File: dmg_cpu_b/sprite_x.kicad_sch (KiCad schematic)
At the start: 88 parts

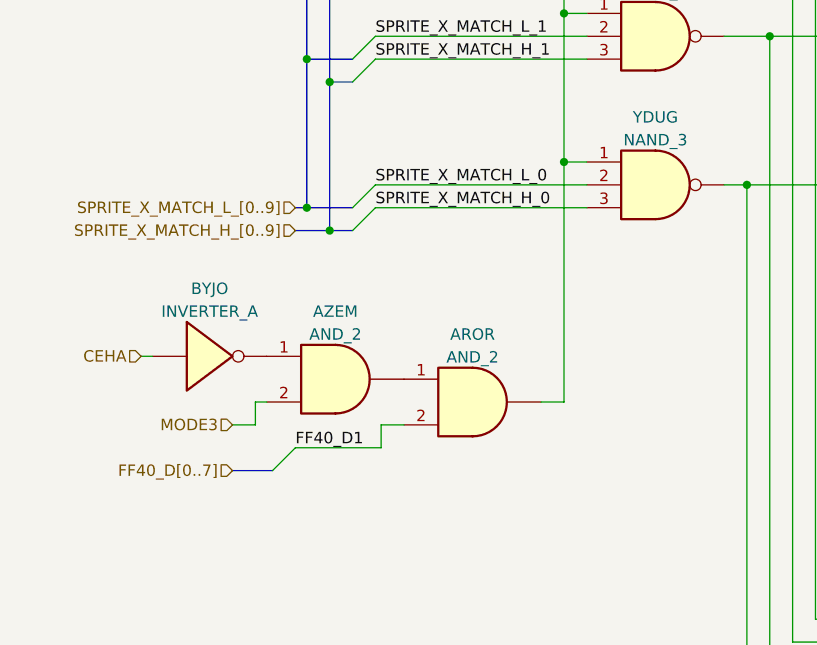
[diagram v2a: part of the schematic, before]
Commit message: More OAM sheets added.
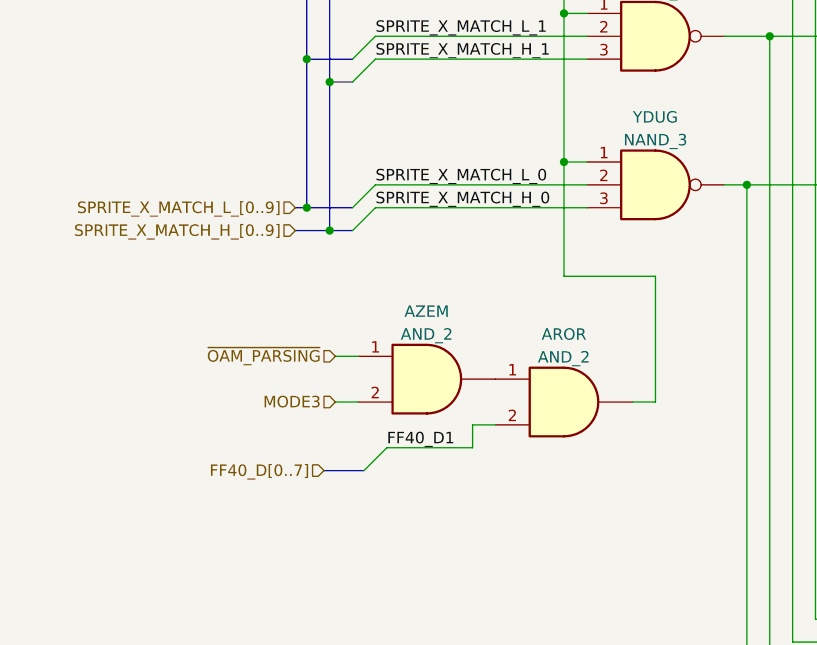
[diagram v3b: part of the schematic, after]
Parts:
- removed BYJO: INVERTER_A, symbol DMG_CPU_Cells:INVERTER_A
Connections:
- net ~{OAM_PARSING}: now reaches AZEM.1
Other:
- moved on the sheet: AROR, AZEM
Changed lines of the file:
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@@
   (junction (at 275.59 61.595) (diameter 0) (color 0 0 0 0)
   )
+  (junction (at 69.215 191.135) (diameter 0) (color 0 0 0 0)
+  )
   (junction (at 40.64 113.665) (diameter 0) (color 0 0 0 0)
   )
@@
   )
   (junction (at 115.57 193.675) (diameter 0) (color 0 0 0 0)
-  )
-  (junction (at 69.215 191.135) (diameter 0) (color 0 0 0 0)
   )
   (junction (at 69.215 92.075) (diameter 0) (color 0 0 0 0)
@@
     (stroke (width 0) (type default) (color 0 0 0 0))
   )
-  (bus_entry (at 39.37 222.885) (size -2.54 2.54)
+  (bus_entry (at 49.53 222.885) (size -2.54 2.54)
     (stroke (width 0) (type default) (color 0 0 0 0))
   )
@@
     (stroke (width 0) (type default) (color 0 0 0 0))
   )
-  (wire (pts (xy 66.675 217.805) (xy 69.215 217.805))
-    (stroke (width 0) (type default) (color 0 0 0 0))
-  )
   (wire (pts (xy 381.635 202.565) (xy 368.3 202.565))
     (stroke (width 0) (type default) (color 0 0 0 0))
@@
     (stroke (width 0) (type default) (color 0 0 0 0))
   )
-  (wire (pts (xy 32.385 220.345) (xy 34.925 220.345))
-    (stroke (width 0) (type default) (color 0 0 0 0))
-  )
   (wire (pts (xy 275.59 73.025) (xy 278.13 73.025))
     (stroke (width 0) (type default) (color 0 0 0 0))
@@
     (stroke (width 0) (type default) (color 0 0 0 0))
   )
+  (wire (pts (xy 79.375 203.835) (xy 79.375 217.805))
+    (stroke (width 0) (type default) (color 0 0 0 0))
+  )
   (wire (pts (xy 312.42 108.585) (xy 312.42 92.075))
     (stroke (width 0) (type default) (color 0 0 0 0))
@@
     (stroke (width 0) (type default) (color 0 0 0 0))
   )
+  (wire (pts (xy 79.375 217.805) (xy 76.835 217.805))
+    (stroke (width 0) (type default) (color 0 0 0 0))
+  )
   (wire (pts (xy 69.215 141.605) (xy 69.215 125.095))
     (stroke (width 0) (type default) (color 0 0 0 0))
@@
     (stroke (width 0) (type default) (color 0 0 0 0))
   )
-  (wire (pts (xy 34.925 220.345) (xy 34.925 217.805))
+  (wire (pts (xy 43.815 217.805) (xy 46.355 217.805))
     (stroke (width 0) (type default) (color 0 0 0 0))
   )
@@
     (stroke (width 0) (type default) (color 0 0 0 0))
   )
-  (wire (pts (xy 22.225 212.725) (xy 23.495 212.725))
+  (wire (pts (xy 43.815 212.725) (xy 46.355 212.725))
     (stroke (width 0) (type default) (color 0 0 0 0))
   )
@@
     (stroke (width 0) (type default) (color 0 0 0 0))
   )
+  (wire (pts (xy 69.215 203.835) (xy 79.375 203.835))
+    (stroke (width 0) (type default) (color 0 0 0 0))
+  )
   (wire (pts (xy 335.28 155.575) (xy 340.36 155.575))
     (stroke (width 0) (type default) (color 0 0 0 0))
@@
     (stroke (width 0) (type default) (color 0 0 0 0))
   )
-  (wire (pts (xy 34.925 217.805) (xy 36.195 217.805))
-    (stroke (width 0) (type default) (color 0 0 0 0))
-  )
   (wire (pts (xy 48.26 160.655) (xy 71.755 160.655))
     (stroke (width 0) (type default) (color 0 0 0 0))
@@
     (stroke (width 0) (type default) (color 0 0 0 0))
   )
-  (bus (pts (xy 32.385 225.425) (xy 36.83 225.425))
+  (bus (pts (xy 42.545 225.425) (xy 46.99 225.425))
     (stroke (width 0) (type default) (color 0 0 0 0))
   )
@@
     (stroke (width 0) (type default) (color 0 0 0 0))
   )
-  (wire (pts (xy 39.37 222.885) (xy 48.895 222.885))
+  (wire (pts (xy 49.53 222.885) (xy 59.055 222.885))
     (stroke (width 0) (type default) (color 0 0 0 0))
   )
@@
     (stroke (width 0) (type default) (color 0 0 0 0))
   )
-  (wire (pts (xy 51.435 220.345) (xy 48.895 220.345))
+  (wire (pts (xy 61.595 220.345) (xy 59.055 220.345))
     (stroke (width 0) (type default) (color 0 0 0 0))
   )
@@
     (stroke (width 0) (type default) (color 0 0 0 0))
   )
-  (wire (pts (xy 69.215 217.805) (xy 69.215 191.135))
-    (stroke (width 0) (type default) (color 0 0 0 0))
-  )
   (wire (pts (xy 71.755 75.565) (xy 69.215 75.565))
     (stroke (width 0) (type default) (color 0 0 0 0))
@@
     (stroke (width 0) (type default) (color 0 0 0 0))
   )
+  (wire (pts (xy 69.215 191.135) (xy 69.215 203.835))
+    (stroke (width 0) (type default) (color 0 0 0 0))
+  )
   (wire (pts (xy 151.13 186.055) (xy 129.54 186.055))
     (stroke (width 0) (type default) (color 0 0 0 0))
@@
     (stroke (width 0) (type default) (color 0 0 0 0))
   )
-  (wire (pts (xy 48.895 220.345) (xy 48.895 222.885))
+  (wire (pts (xy 59.055 220.345) (xy 59.055 222.885))
     (stroke (width 0) (type default) (color 0 0 0 0))
   )
@@
     (stroke (width 0) (type default) (color 0 0 0 0))
   )
-  (label "FF40_D1" (at 39.37 222.885 0)
+  (label "FF40_D1" (at 49.53 222.885 0)
     (effects (font (size 1.27 1.27)) (justify left bottom))
   )
@@
     (effects (font (size 1.27 1.27)) (justify left))
   )
-  (hierarchical_label "CEHA" (shape input) (at 22.225 212.725 180)
+  (hierarchical_label "~{OAM_PARSING}" (shape input) (at 43.815 212.725 180)
     (effects (font (size 1.27 1.27)) (justify right))
   )
@@
     (effects (font (size 1.27 1.27)) (justify left))
   )
-  (hierarchical_label "FF40_D[0..7]" (shape input) (at 32.385 225.425 180)
+  (hierarchical_label "FF40_D[0..7]" (shape input) (at 42.545 225.425 180)
     (effects (font (size 1.27 1.27)) (justify right))
   )
-  (hierarchical_label "MODE3" (shape input) (at 32.385 220.345 180)
+  (hierarchical_label "MODE3" (shape input) (at 43.815 217.805 180)
     (effects (font (size 1.27 1.27)) (justify right))
   )
@@
     (pin "6")
   )
-  (symbol (lib_id "DMG_CPU_Cells:INVERTER_A") (at 29.845 212.725 0) (unit 1)
-    (in_bom yes) (on_board yes) (fields_autoplaced)
-    (property "Reference" "BYJO" (id 0) (at 29.845 205.2152 0))
-    (property "Value" "INVERTER_A" (id 1) (at 29.845 207.7521 0))
-    (property "Footprint" "" (id 2) (at 27.305 212.725 0)
-      (effects (font (size 1.27 1.27)) hide)
-    )
-    (property "Datasheet" "http://iceboy.a-singer.de/doc/dmg_cells.html#inv_a" (id 3) (at 31.115 220.345 0)
-      (effects (font (size 1.27 1.27)) hide)
-    )
-    (pin "1")
-    (pin "2")
-  )
   (symbol (lib_id "DMG_CPU_Cells:NAND_3") (at 79.375 144.145 0) (unit 1)
     (in_bom yes) (on_board yes) (fields_autoplaced)
@@
     (pin "4")
   )
-  (symbol (lib_id "DMG_CPU_Cells:AND_2") (at 59.055 217.805 0) (unit 1)
-    (in_bom yes) (on_board yes) (fields_autoplaced)
-    (property "Reference" "AROR" (id 0) (at 59.055 210.2952 0))
-    (property "Value" "AND_2" (id 1) (at 59.055 212.8321 0))
-    (property "Footprint" "" (id 2) (at 59.055 217.805 0)
-      (effects (font (size 1.27 1.27)) hide)
-    )
-    (property "Datasheet" "http://iceboy.a-singer.de/doc/dmg_cells.html#and2" (id 3) (at 59.055 225.425 0)
+  (symbol (lib_id "DMG_CPU_Cells:AND_2") (at 69.215 217.805 0) (unit 1)
+    (in_bom yes) (on_board yes) (fields_autoplaced)
+    (property "Reference" "AROR" (id 0) (at 69.215 210.2952 0))
+    (property "Value" "AND_2" (id 1) (at 69.215 212.8321 0))
+    (property "Footprint" "" (id 2) (at 69.215 217.805 0)
+      (effects (font (size 1.27 1.27)) hide)
+    )
+    (property "Datasheet" "http://iceboy.a-singer.de/doc/dmg_cells.html#and2" (id 3) (at 69.215 225.425 0)
       (effects (font (size 1.27 1.27)) hide)
     )
@@
     (pin "2")
   )
-  (symbol (lib_id "DMG_CPU_Cells:AND_2") (at 43.815 215.265 0) (unit 1)
-    (in_bom yes) (on_board yes) (fields_autoplaced)
-    (property "Reference" "AZEM" (id 0) (at 43.815 207.7552 0))
-    (property "Value" "AND_2" (id 1) (at 43.815 210.2921 0))
-    (property "Footprint" "" (id 2) (at 43.815 215.265 0)
-      (effects (font (size 1.27 1.27)) hide)
-    )
-    (property "Datasheet" "http://iceboy.a-singer.de/doc/dmg_cells.html#and2" (id 3) (at 43.815 222.885 0)
-      (effects (font (size 1.27 1.27)) hide)
-    )
+  (symbol (lib_id "DMG_CPU_Cells:AND_2") (at 53.975 215.265 0) (unit 1)
+    (in_bom yes) (on_board yes) (fields_autoplaced)
+    (property "Reference" "AZEM" (id 0) (at 53.975 207.7552 0))
+    (property "Value" "AND_2" (id 1) (at 53.975 210.2921 0))
+    (property "Footprint" "" (id 2) (at 53.975 215.265 0)
+      (effects (font (size 1.27 1.27)) hide)
+    )
+    (property "Datasheet" "http://iceboy.a-singer.de/doc/dmg_cells.html#and2" (id 3) (at 53.975 222.885 0)
+      (effects (font (size 1.27 1.27)) hide)
+    )

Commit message: All sheets captured. Serious tidying is required in PPU section.
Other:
- company: (none) -> CC-BY-SA-4.0 Régis Galland & Michael Singer -- Derived work from Furrtek
- title: (none) -> DMG CPU B
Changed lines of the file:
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@@
 (kicad_sch (version 20211123) (generator eeschema)
   (paper "A3")
+  (title_block
+    (title "DMG CPU B")
+    (date "2022-05-19")
+    (rev "0")
+    (company "CC-BY-SA-4.0 Régis Galland & Michael Singer -- Derived work from Furrtek")
+    (comment 1 "https://github.com/msinger/dmg-schematics")
+  )
   (junction (at 337.82 100.965) (diameter 0) (color 0 0 0 0)
   )

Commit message: Changes made on review.
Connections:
- net ~{RESET_VIDEO} renamed ~{PPU_RESET}
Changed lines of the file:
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@@
     (effects (font (size 1.27 1.27)) (justify right))
   )
-  (hierarchical_label "~{RESET_VIDEO}" (shape input) (at 256.54 34.29 180)
+  (hierarchical_label "~{PPU_RESET}" (shape input) (at 256.54 34.29 180)
     (effects (font (size 1.27 1.27)) (justify right))
   )

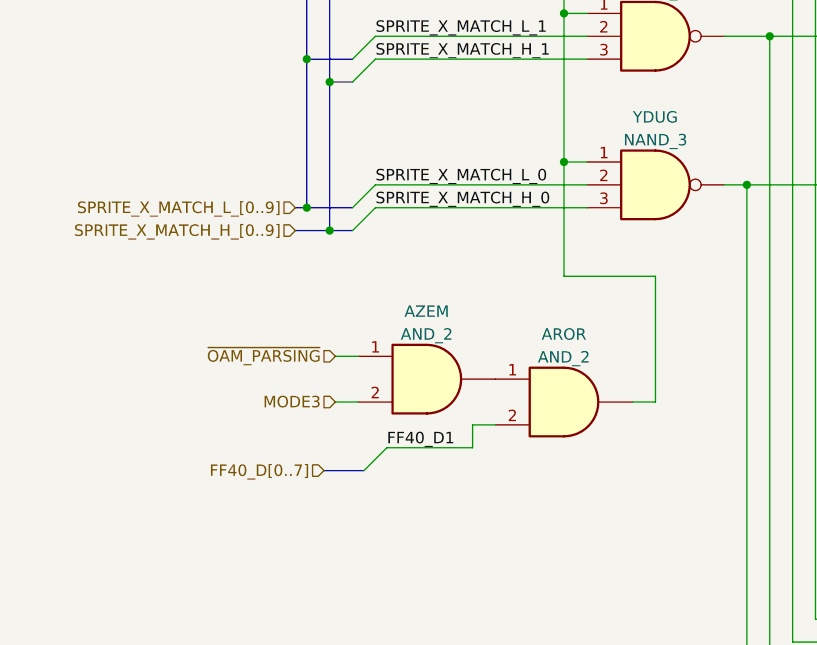
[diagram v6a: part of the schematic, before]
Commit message: Elements from sptite control sheet moved to lcd sheet.
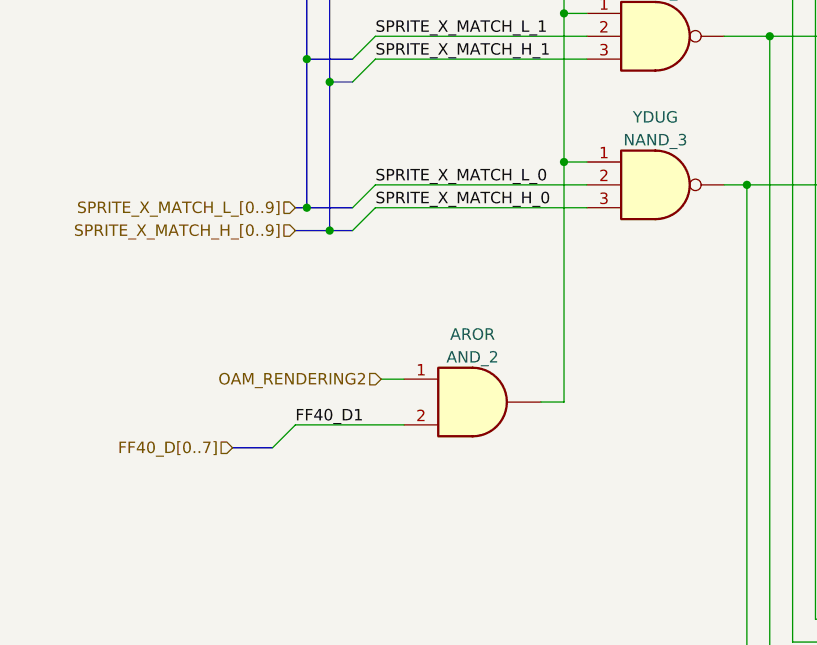
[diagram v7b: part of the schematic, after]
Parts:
- removed AZEM: AND_2, symbol DMG_CPU_Cells:AND_2
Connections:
- net OAM_RENDERING2: now reaches AROR.1
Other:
- moved on the sheet: AROR
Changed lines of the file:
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@@
     (stroke (width 0) (type default) (color 0 0 0 0))
   )
-  (bus_entry (at 49.53 222.885) (size -2.54 2.54)
+  (bus_entry (at 39.37 220.345) (size -2.54 2.54)
     (stroke (width 0) (type default) (color 0 0 0 0))
   )
@@
     (stroke (width 0) (type default) (color 0 0 0 0))
   )
-  (wire (pts (xy 79.375 203.835) (xy 79.375 217.805))
-    (stroke (width 0) (type default) (color 0 0 0 0))
-  )
   (wire (pts (xy 312.42 108.585) (xy 312.42 92.075))
     (stroke (width 0) (type default) (color 0 0 0 0))
@@
     (stroke (width 0) (type default) (color 0 0 0 0))
   )
-  (wire (pts (xy 79.375 217.805) (xy 76.835 217.805))
+  (wire (pts (xy 69.215 217.805) (xy 66.675 217.805))
     (stroke (width 0) (type default) (color 0 0 0 0))
   )
@@
     (stroke (width 0) (type default) (color 0 0 0 0))
   )
-  (wire (pts (xy 43.815 217.805) (xy 46.355 217.805))
-    (stroke (width 0) (type default) (color 0 0 0 0))
-  )
   (wire (pts (xy 220.98 103.505) (xy 220.98 108.585))
     (stroke (width 0) (type default) (color 0 0 0 0))
@@
     (stroke (width 0) (type default) (color 0 0 0 0))
   )
-  (wire (pts (xy 43.815 212.725) (xy 46.355 212.725))
+  (wire (pts (xy 48.895 215.265) (xy 51.435 215.265))
     (stroke (width 0) (type default) (color 0 0 0 0))
   )
@@
     (stroke (width 0) (type default) (color 0 0 0 0))
   )
-  (wire (pts (xy 69.215 203.835) (xy 79.375 203.835))
-    (stroke (width 0) (type default) (color 0 0 0 0))
-  )
   (wire (pts (xy 335.28 155.575) (xy 340.36 155.575))
     (stroke (width 0) (type default) (color 0 0 0 0))
@@
     (stroke (width 0) (type default) (color 0 0 0 0))
   )
-  (bus (pts (xy 42.545 225.425) (xy 46.99 225.425))
+  (bus (pts (xy 32.385 222.885) (xy 36.83 222.885))
     (stroke (width 0) (type default) (color 0 0 0 0))
   )
@@
     (stroke (width 0) (type default) (color 0 0 0 0))
   )
-  (wire (pts (xy 49.53 222.885) (xy 59.055 222.885))
-    (stroke (width 0) (type default) (color 0 0 0 0))
-  )
   (wire (pts (xy 275.59 127.635) (xy 275.59 122.555))
     (stroke (width 0) (type default) (color 0 0 0 0))
@@
     (stroke (width 0) (type default) (color 0 0 0 0))
   )
-  (wire (pts (xy 61.595 220.345) (xy 59.055 220.345))
+  (wire (pts (xy 39.37 220.345) (xy 51.435 220.345))
     (stroke (width 0) (type default) (color 0 0 0 0))
   )
@@
     (stroke (width 0) (type default) (color 0 0 0 0))
   )
-  (wire (pts (xy 69.215 191.135) (xy 69.215 203.835))
+  (wire (pts (xy 69.215 191.135) (xy 69.215 217.805))
     (stroke (width 0) (type default) (color 0 0 0 0))
   )
@@
     (stroke (width 0) (type default) (color 0 0 0 0))
   )
-  (wire (pts (xy 59.055 220.345) (xy 59.055 222.885))
-    (stroke (width 0) (type default) (color 0 0 0 0))
-  )
   (wire (pts (xy 275.59 94.615) (xy 275.59 89.535))
     (stroke (width 0) (type default) (color 0 0 0 0))
@@
     (stroke (width 0) (type default) (color 0 0 0 0))
   )
-  (label "FF40_D1" (at 49.53 222.885 0)
+  (label "FF40_D1" (at 39.37 220.345 0)
     (effects (font (size 1.27 1.27)) (justify left bottom))
   )
@@
     (effects (font (size 1.27 1.27)) (justify left))
   )
-  (hierarchical_label "~{OAM_PARSING}" (shape input) (at 43.815 212.725 180)
+  (hierarchical_label "OAM_RENDERING2" (shape input) (at 48.895 215.265 180)
     (effects (font (size 1.27 1.27)) (justify right))
   )
@@
     (effects (font (size 1.27 1.27)) (justify left))
   )
-  (hierarchical_label "FF40_D[0..7]" (shape input) (at 42.545 225.425 180)
-    (effects (font (size 1.27 1.27)) (justify right))
-  )
-  (hierarchical_label "MODE3" (shape input) (at 43.815 217.805 180)
+  (hierarchical_label "FF40_D[0..7]" (shape input) (at 32.385 222.885 180)
     (effects (font (size 1.27 1.27)) (justify right))
   )
@@
     (pin "4")
   )
-  (symbol (lib_id "DMG_CPU_Cells:AND_2") (at 69.215 217.805 0) (unit 1)
-    (in_bom yes) (on_board yes) (fields_autoplaced)
-    (property "Reference" "AROR" (id 0) (at 69.215 210.2952 0))
-    (property "Value" "AND_2" (id 1) (at 69.215 212.8321 0))
-    (property "Footprint" "" (id 2) (at 69.215 217.805 0)
-      (effects (font (size 1.27 1.27)) hide)
-    )
-    (property "Datasheet" "http://iceboy.a-singer.de/doc/dmg_cells.html#and2" (id 3) (at 69.215 225.425 0)
+  (symbol (lib_id "DMG_CPU_Cells:AND_2") (at 59.055 217.805 0) (unit 1)
+    (in_bom yes) (on_board yes) (fields_autoplaced)
+    (property "Reference" "AROR" (id 0) (at 59.055 210.2952 0))
+    (property "Value" "AND_2" (id 1) (at 59.055 212.8321 0))
+    (property "Footprint" "" (id 2) (at 59.055 217.805 0)
+      (effects (font (size 1.27 1.27)) hide)
+    )
+    (property "Datasheet" "http://iceboy.a-singer.de/doc/dmg_cells.html#and2" (id 3) (at 59.055 225.425 0)
       (effects (font (size 1.27 1.27)) hide)
     )
@@
     (pin "2")
   )
-  (symbol (lib_id "DMG_CPU_Cells:AND_2") (at 53.975 215.265 0) (unit 1)
-    (in_bom yes) (on_board yes) (fields_autoplaced)
-    (property "Reference" "AZEM" (id 0) (at 53.975 207.7552 0))
-    (property "Value" "AND_2" (id 1) (at 53.975 210.2921 0))
-    (property "Footprint" "" (id 2) (at 53.975 215.265 0)
-      (effects (font (size 1.27 1.27)) hide)
-    )
-    (property "Datasheet" "http://iceboy.a-singer.de/doc/dmg_cells.html#and2" (id 3) (at 53.975 222.885 0)
-      (effects (font (size 1.27 1.27)) hide)
-    )
-    (pin "1")
-    (pin "2")
-    (pin "3")
-  )
   (symbol (lib_id "DMG_CPU_Cells:OR_2") (at 236.22 80.645 0) (unit 1)

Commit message: Quite a few fixes from review.
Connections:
- net at FEFY.6: now also FEPO.1; no longer FEPO.2
- net at FOVE.6: now also FEPO.2; no longer FEPO.1
- net SPRITE_RST_0 renamed SPRITE_RST0
- net SPRITE_RST_1 renamed SPRITE_RST1
- net SPRITE_RST_2 renamed SPRITE_RST2
- net SPRITE_RST_3 renamed SPRITE_RST3
- net SPRITE_RST_4 renamed SPRITE_RST4
- net SPRITE_RST_5 renamed SPRITE_RST5
- net SPRITE_RST_6 renamed SPRITE_RST6
- net SPRITE_RST_7 renamed SPRITE_RST7
- net SPRITE_RST_8 renamed SPRITE_RST8
- net SPRITE_RST_9 renamed SPRITE_RST9
- net SPRITE_SEL_0 renamed SPRITE_SEL0
- net SPRITE_SEL_1 renamed SPRITE_SEL1
- net SPRITE_SEL_2 renamed SPRITE_SEL2
- net SPRITE_SEL_3 renamed SPRITE_SEL3
- net SPRITE_SEL_4 renamed SPRITE_SEL4
- net SPRITE_SEL_5 renamed SPRITE_SEL5
- net SPRITE_SEL_6 renamed SPRITE_SEL6
- net SPRITE_SEL_7 renamed SPRITE_SEL7
- net SPRITE_SEL_8 renamed SPRITE_SEL8
- net SPRITE_SEL_9 renamed SPRITE_SEL9
- net SPRITE_X_MATCH_H_0 renamed SPRITE_X_MATCH_H0
- net SPRITE_X_MATCH_H_1 renamed SPRITE_X_MATCH_H1
- net SPRITE_X_MATCH_H_2 renamed SPRITE_X_MATCH_H2
- net SPRITE_X_MATCH_H_3 renamed SPRITE_X_MATCH_H3
- net SPRITE_X_MATCH_H_4 renamed SPRITE_X_MATCH_H4
- net SPRITE_X_MATCH_H_5 renamed SPRITE_X_MATCH_H5
- net SPRITE_X_MATCH_H_6 renamed SPRITE_X_MATCH_H6
- net SPRITE_X_MATCH_H_7 renamed SPRITE_X_MATCH_H7
- net SPRITE_X_MATCH_H_8 renamed SPRITE_X_MATCH_H8
- net SPRITE_X_MATCH_H_9 renamed SPRITE_X_MATCH_H9
- net SPRITE_X_MATCH_L_0 renamed SPRITE_X_MATCH_L0
- net SPRITE_X_MATCH_L_1 renamed SPRITE_X_MATCH_L1
- net SPRITE_X_MATCH_L_2 renamed SPRITE_X_MATCH_L2
- net SPRITE_X_MATCH_L_3 renamed SPRITE_X_MATCH_L3
- net SPRITE_X_MATCH_L_4 renamed SPRITE_X_MATCH_L4
- net SPRITE_X_MATCH_L_5 renamed SPRITE_X_MATCH_L5
- net SPRITE_X_MATCH_L_6 renamed SPRITE_X_MATCH_L6
- net SPRITE_X_MATCH_L_7 renamed SPRITE_X_MATCH_L7
- net SPRITE_X_MATCH_L_8 renamed SPRITE_X_MATCH_L8
- net SPRITE_X_MATCH_L_9 renamed SPRITE_X_MATCH_L9
